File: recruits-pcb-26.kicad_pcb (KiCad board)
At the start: 4 copper layers, 57.7 x 24.4 mm, 34 parts, among them Q1 AO3401A, Q2 AO3401A, SW1 TS3425BA, SW2 TS3425BA, U3 STM32C011F4P6TR, U4 LSM6DSVETR, U5 CH340N, U6 ME6231A33M3G, U7 AT25640B-SSHL-T, U8 XY308-2.54-2P

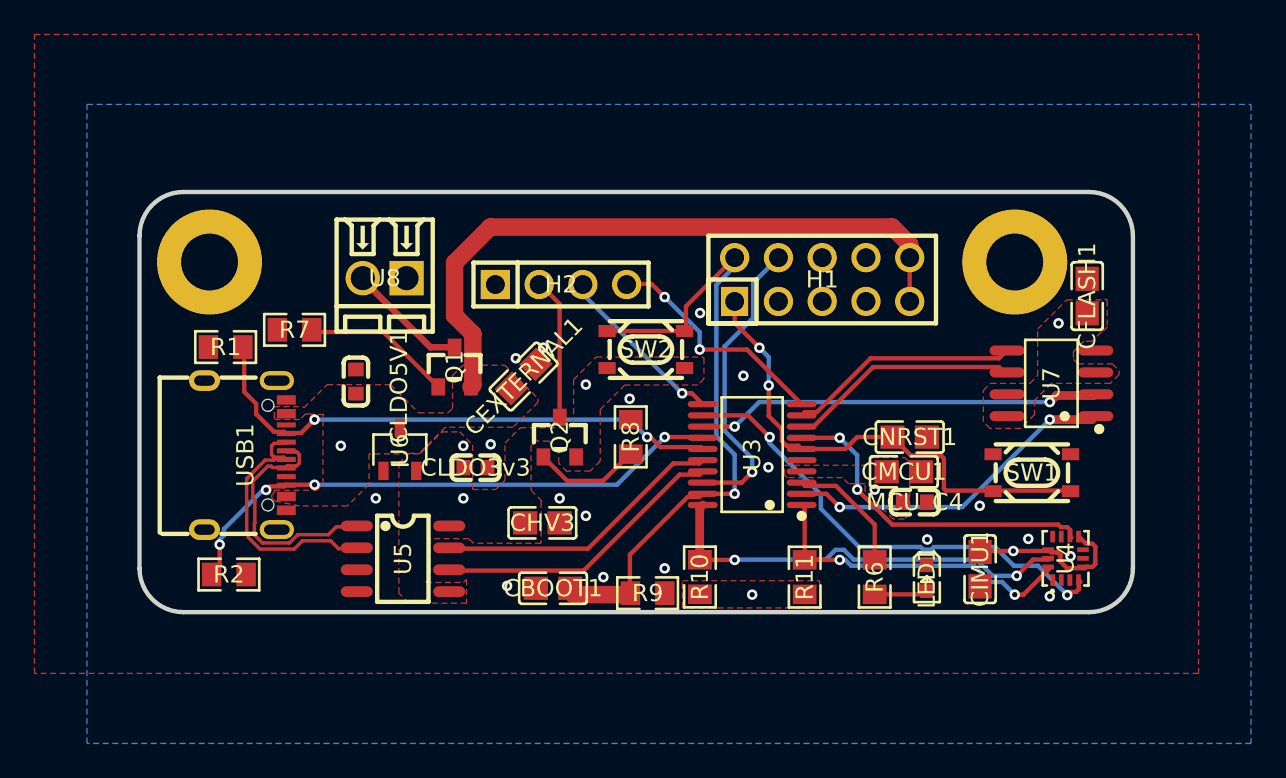
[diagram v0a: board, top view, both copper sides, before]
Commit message: removed traces and routing
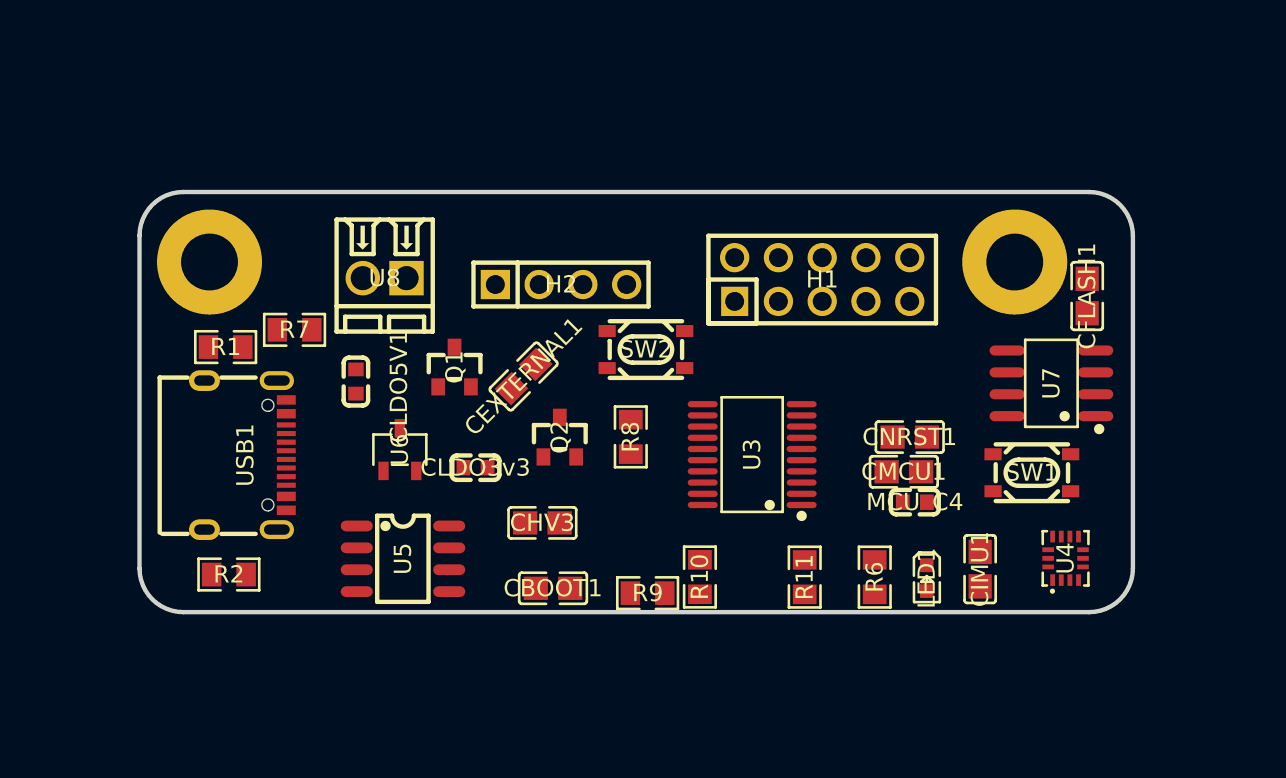
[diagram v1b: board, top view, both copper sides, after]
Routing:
- net 5V: track 38.7 -> 0.00 mm
- net SWDCLK-BOOT0: track 38.0 -> 0.00 mm, vias 1 -> 0
- net USB_CC2: track 32.4 -> 0.00 mm, vias 4 -> 0
- net USB_CC1: track 31.4 -> 0.00 mm, vias 2 -> 0
- net NRST: track 28.8 -> 0.00 mm, vias 2 -> 0
- net IMU_INT1: track 27.6 -> 0.00 mm, vias 2 -> 0
- net SCL: track 24.8 -> 0.00 mm, vias 2 -> 0
- net SPI_MISO: track 23.5 -> 0.00 mm, vias 2 -> 0
- net IMU_INT2: track 19.5 -> 0.00 mm, vias 2 -> 0
- net FLASH_CS: track 19.4 -> 0.00 mm, vias 2 -> 0
- net SDA: track 19.0 -> 0.00 mm, vias 2 -> 0
- net SWDIO: track 17.5 -> 0.00 mm, vias 1 -> 0
- net USB_TXD: track 17.2 -> 0.00 mm
- net USB_RXD: track 16.9 -> 0.00 mm
- net /USB-: track 15.4 -> 0.00 mm
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- removed copper zone on F.Cu, net 3V3
- removed copper zone on In1.Cu, net 3V3
- removed copper zone on F.Cu, net 5V
- removed copper zone on B.Cu, net GND
- removed copper zone on F.Cu, net GND
- removed copper zone on In2.Cu, net GND

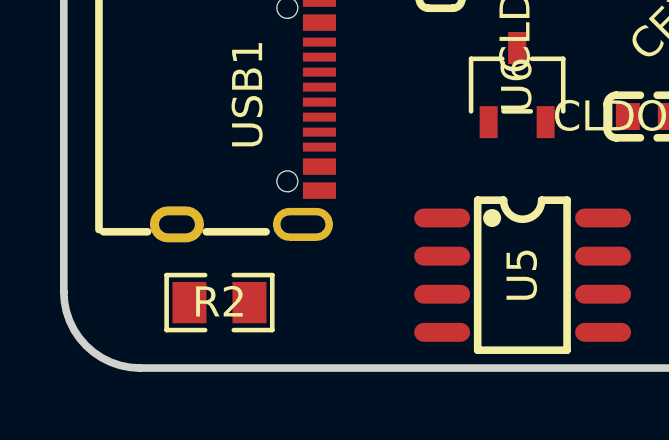
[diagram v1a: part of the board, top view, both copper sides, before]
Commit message: added dp constraints
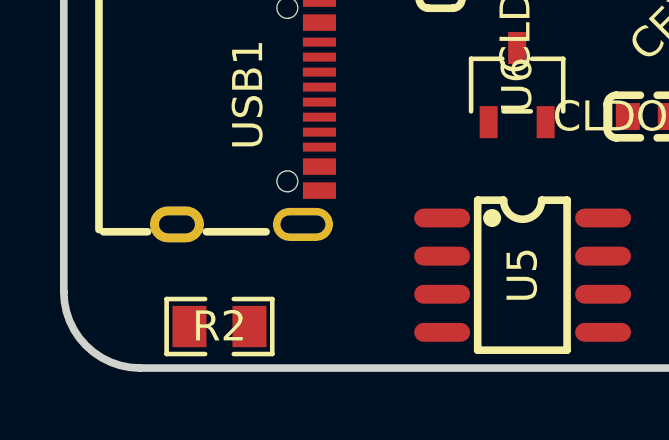
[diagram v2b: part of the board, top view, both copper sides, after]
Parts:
- moved R2 0.80 mm to (125.2, 113.0)
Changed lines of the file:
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@@
 	)
 	(setup
+		(stackup
+			(layer "F.SilkS"
+				(type "Top Silk Screen")
+			)
+			(layer "F.Paste"
+				(type "Top Solder Paste")
+			)
+			(layer "F.Mask"
+				(type "Top Solder Mask")
+				(thickness 0.01)
+			)
+			(layer "F.Cu"
+				(type "copper")
+				(thickness 0.035)
+			)
+			(layer "dielectric 1"
+				(type "core")
+				(thickness 0.48)
+				(material "FR4")
+				(epsilon_r 4.5)
+				(loss_tangent 0.02)
+			)
+			(layer "In1.Cu"
+				(type "copper")
+				(thickness 0.035)
+			)
+			(layer "dielectric 2"
+				(type "prepreg")
+				(thickness 0.48)
+				(material "FR4")
+				(epsilon_r 4.5)
+				(loss_tangent 0.02)
+			)
+			(layer "In2.Cu"
+				(type "copper")
+				(thickness 0.035)
+			)
+			(layer "dielectric 3"
+				(type "core")
+				(thickness 0.48)
+				(material "FR4")
+				(epsilon_r 4.5)
+				(loss_tangent 0.02)
+			)
+			(layer "B.Cu"
+				(type "copper")
+				(thickness 0.035)
+			)
+			(layer "B.Mask"
+				(type "Bottom Solder Mask")
+				(thickness 0.01)
+			)
+			(layer "B.Paste"
+				(type "Bottom Solder Paste")
+			)
+			(layer "B.SilkS"
+				(type "Bottom Silk Screen")
+			)
+			(copper_finish "None")
+			(dielectric_constraints no)
+		)
 		(pad_to_mask_clearance 0)
 		(allow_soldermask_bridges_in_footprints no)
@@
 		(capping no)
 		(filling no)
+		(zone_defaults)
 		(aux_axis_origin 120 90)
 		(pcbplotparams
@@
 	(footprint "ProPrj_test1_2026-09-10-import-fps:R0805"
 		(layer "F.Cu")
-		(at 125.188318 112.201829 180)
+		(at 125.188318 113 180)
 		(property "Reference" "R2"
 			(at 0 0 0)
